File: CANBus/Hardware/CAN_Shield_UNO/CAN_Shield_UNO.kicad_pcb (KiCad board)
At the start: 2 copper layers, 68.6 x 53.3 mm, 39 parts, among them J1 Power, J2 Digital/PWM, J3 Analog, J4 Digital/PWM, J7 Screw_Terminal_01x02, U2 TCAN1051HGV

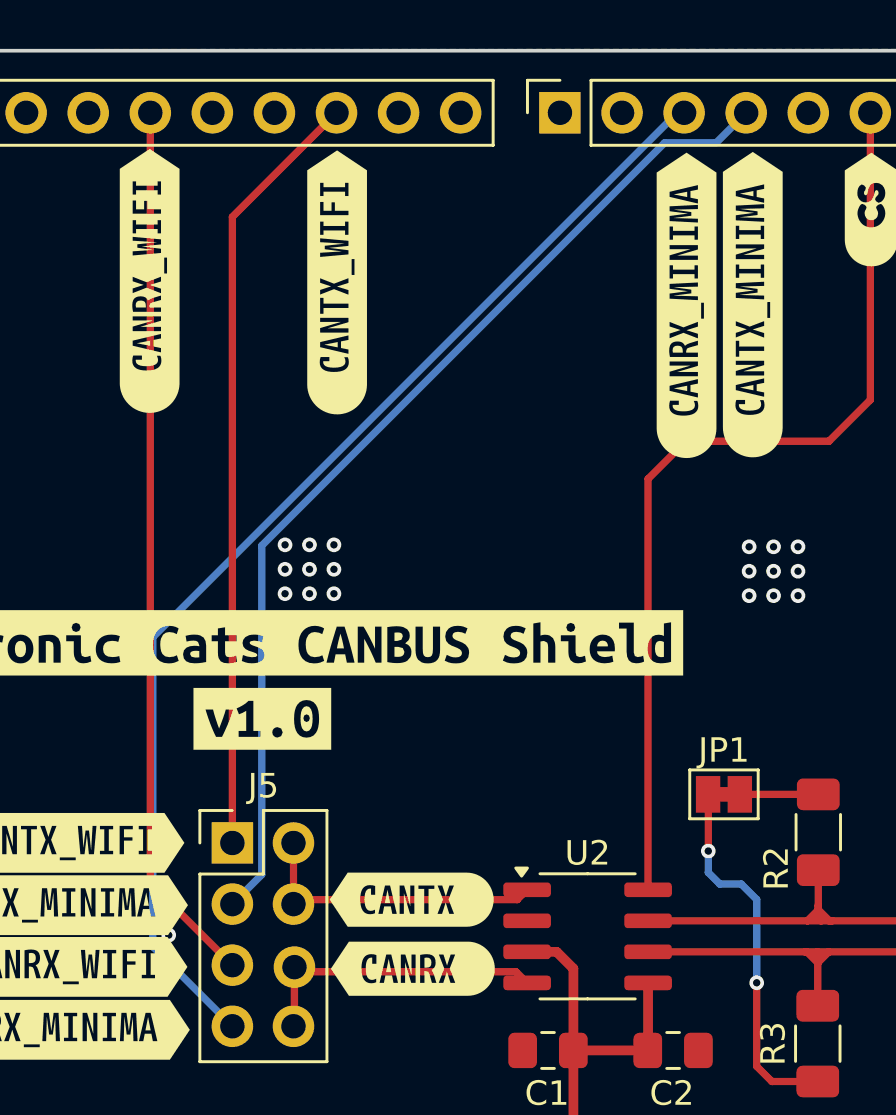
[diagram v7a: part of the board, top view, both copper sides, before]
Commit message: fix: change VIO power supply
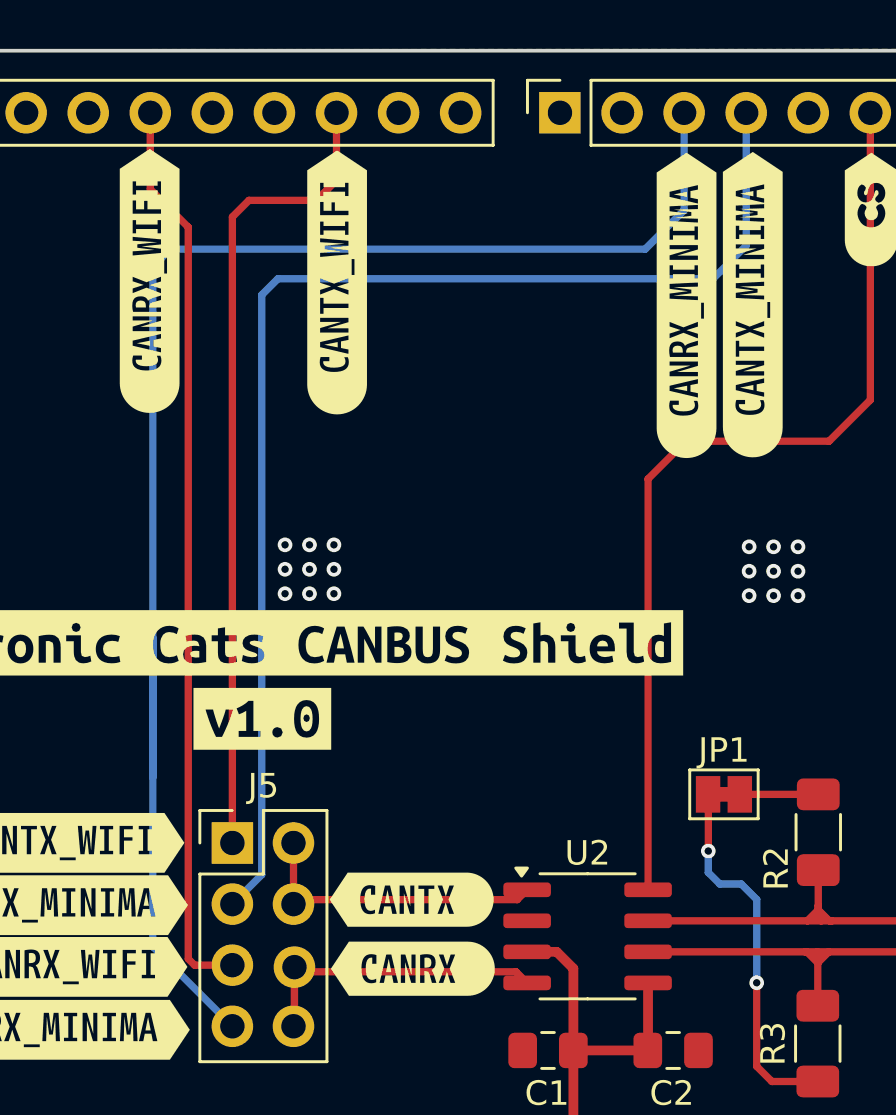
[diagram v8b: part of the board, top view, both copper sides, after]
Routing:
- net /CRX0_MINIMA: track 47.9 -> 65.1 mm
- net /CTX0_MINIMA: track 42.3 -> 51.5 mm
- net /CTX0_WIFI: track 31.6 -> 33.3 mm
- net /CRX0_WIFI: track 36.3 -> 37.2 mm
- net GND: vias 56 -> 55
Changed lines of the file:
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@@
-	)
-	(via
-		(at 129.71 82.85)
-		(size 0.6)
-		(drill 0.3)
-		(layers "F.Cu" "B.Cu")
-		(free yes)
-		(net 1)
 	)
 	(via
@@
 	)
 	(segment
-		(start 132.315 84.08)
-		(end 128.956 80.721)
+		(start 128.956 49.2)
+		(end 128.956 52.326)
 		(width 0.3)
 		(layer "F.Cu")
@@
 	)
 	(segment
-		(start 128.956 80.721)
-		(end 128.956 49.2)
+		(start 130.51 83.82)
+		(end 130.77 84.08)
 		(width 0.3)
 		(layer "F.Cu")
 		(net 11)
+	)
+	(segment
+		(start 128.956 52.326)
+		(end 130.51 53.88)
+		(width 0.3)
+		(layer "F.Cu")
+		(net 11)
+	)
+	(segment
+		(start 130.51 53.88)
+		(end 130.51 83.82)
+		(width 0.3)
+		(layer "F.Cu")
+		(net 11)
+	)
+	(segment
+		(start 130.77 84.08)
+		(end 132.315 84.08)
+		(width 0.3)
+		(layer "F.Cu")
+		(net 11)
+	)
+	(segment
+		(start 132.315 53.461)
+		(end 132.993 52.783)
+		(width 0.3)
+		(layer "F.Cu")
+		(net 17)
+	)
+	(segment
+		(start 135.757 52.783)
+		(end 136.576 51.964)
+		(width 0.3)
+		(layer "F.Cu")
+		(net 17)
+	)
+	(segment
+		(start 136.576 51.964)
+		(end 136.576 49.2)
+		(width 0.3)
+		(layer "F.Cu")
+		(net 17)
+	)
+	(segment
+		(start 132.993 52.783)
+		(end 135.757 52.783)
+		(width 0.3)
+		(layer "F.Cu")
+		(net 17)
 	)
 	(segment
@@
 	)
 	(segment
-		(start 132.315 53.461)
-		(end 136.576 49.2)
-		(width 0.3)
-		(layer "F.Cu")
-		(net 17)
-	)
-	(segment
-		(start 150.005761 50.425)
-		(end 133.515 66.915761)
+		(start 153.34 54.64)
+		(end 153.34 49.2)
 		(width 0.3)
 		(layer "B.Cu")
@@
 	)
 	(segment
-		(start 152.115 50.425)
-		(end 150.005761 50.425)
+		(start 151.99 55.99)
+		(end 153.34 54.64)
 		(width 0.3)
 		(layer "B.Cu")
@@
 	)
 	(segment
+		(start 132.315 81.58)
+		(end 133.515 80.38)
+		(width 0.3)
+		(layer "B.Cu")
+		(net 19)
+	)
+	(segment
+		(start 133.515 56.655)
+		(end 134.18 55.99)
+		(width 0.3)
+		(layer "B.Cu")
+		(net 19)
+	)
+	(segment
 		(start 133.515 80.38)
-		(end 132.315 81.58)
+		(end 133.515 56.655)
 		(width 0.3)
 		(layer "B.Cu")
@@
 	)
 	(segment
-		(start 153.34 49.2)
-		(end 152.115 50.425)
-		(width 0.3)
-		(layer "B.Cu")
-		(net 19)
-	)
-	(segment
-		(start 133.515 66.915761)
-		(end 133.515 80.38)
+		(start 134.18 55.99)
+		(end 151.99 55.99)
 		(width 0.3)
 		(layer "B.Cu")
@@
 	)
 	(segment
-		(start 150.523654 49.2)
-		(end 129.06 70.663655)
+		(start 149.21 54.78)
+		(end 129.78 54.78)
+		(width 0.3)
+		(layer "B.Cu")
+		(net 22)
+	)
+	(segment
+		(start 150.8 53.19)
+		(end 149.21 54.78)
+		(width 0.3)
+		(layer "B.Cu")
+		(net 22)
+	)
+	(segment
+		(start 129.06 83.325)
+		(end 129.06 76.38)
 		(width 0.3)
 		(layer "B.Cu")
@@
 	)
 	(segment
-		(start 129.06 83.325)
+		(start 150.8 49.2)
+		(end 150.8 53.19)
+		(width 0.3)
+		(layer "B.Cu")
+		(net 22)
+	)
+	(segment
+		(start 129.06 55.5)
+		(end 129.06 76.38)
+		(width 0.3)
+		(layer "B.Cu")
+		(net 22)
+	)
+	(segment
+		(start 129.06 76.38)
 		(end 129.06 70.663655)
 		(width 0.3)
@@
 		(width 0.3)
 		(layer "B.Cu")
+		(net 22)
+	)
+	(segment
+		(start 129.78 54.78)
+		(end 129.06 55.5)
+		(width 0.3)
+		(layer "B.Cu")
